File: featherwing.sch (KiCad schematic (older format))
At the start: 3 parts, among them J9 GROVE-SMD-90D, U1 ROF-78E

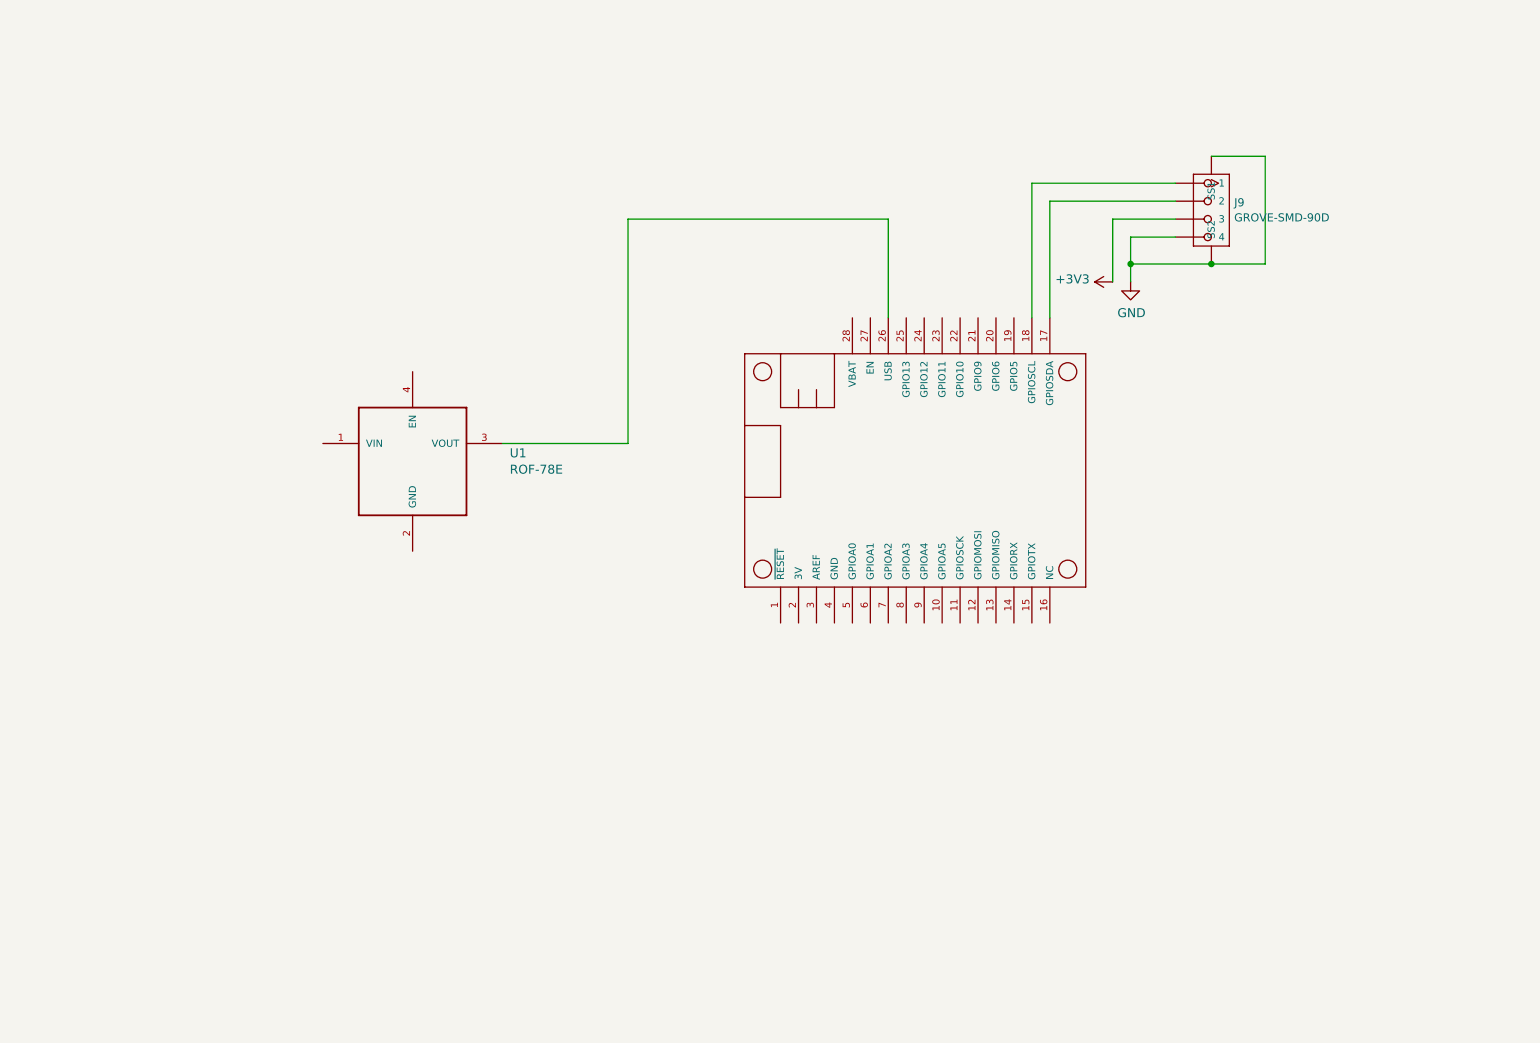
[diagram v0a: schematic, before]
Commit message: Updates from urbito, wired up featherwing
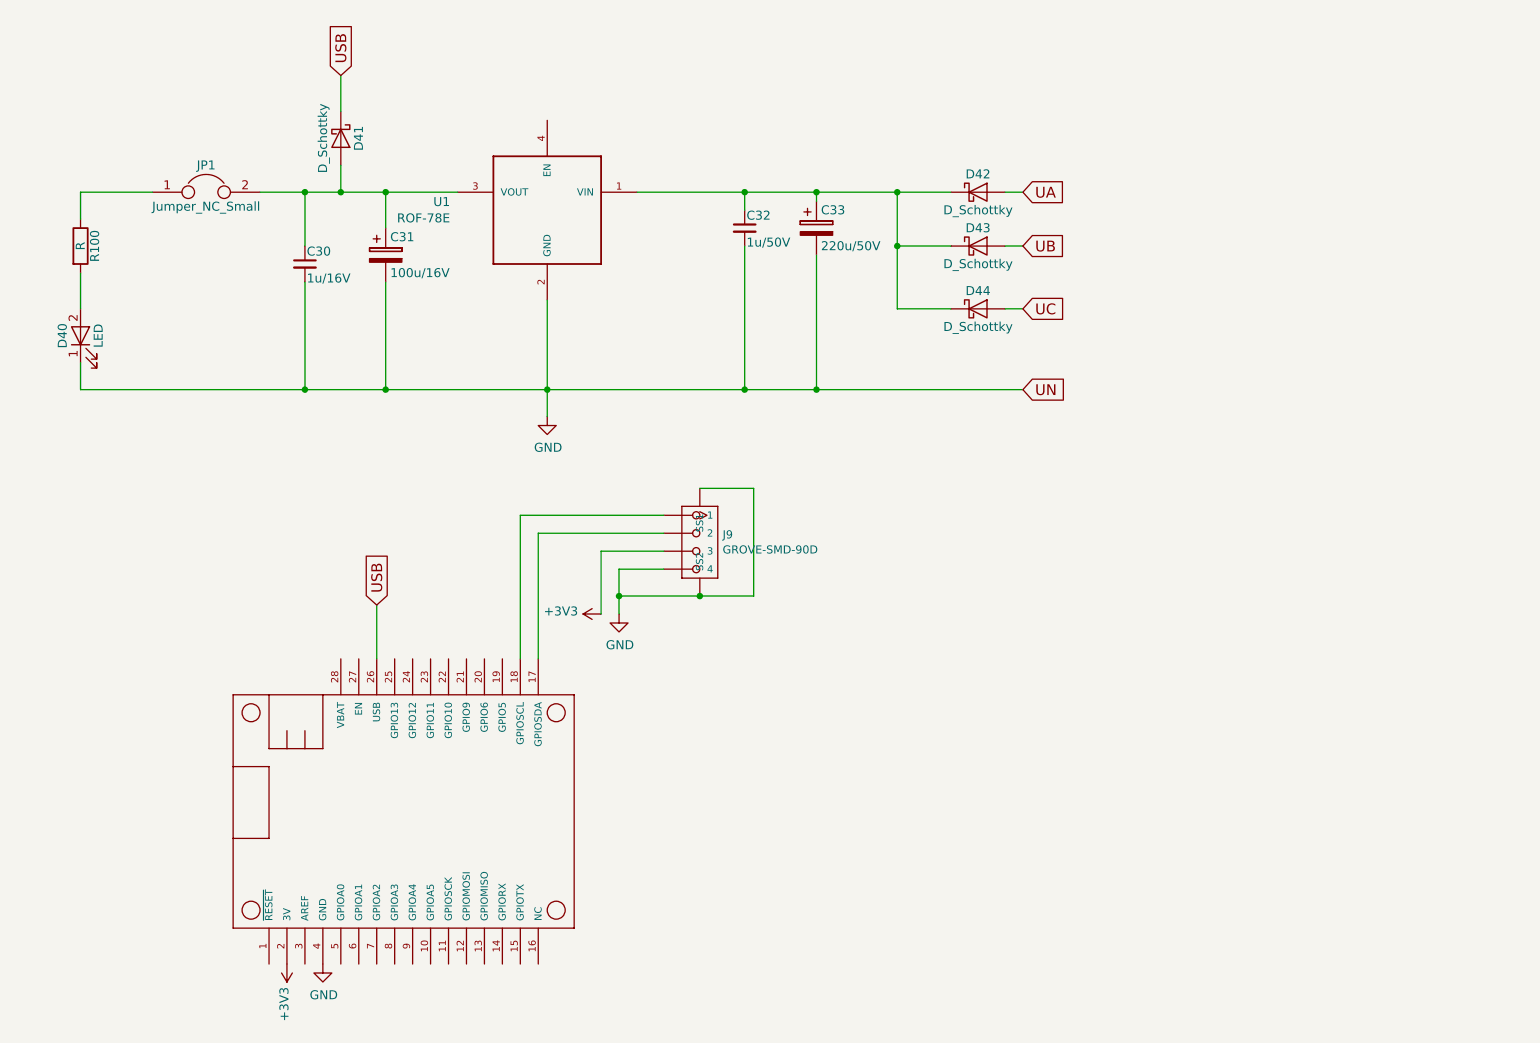
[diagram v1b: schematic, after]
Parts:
- added C30: 1u/16V, Capacitors_SMD:C_0603, symbol C_Small
- added C31: 100u/16V, Capacitors_SMD:CP_Elec_5x5.8, symbol CP
- added C32: 1u/50V, Capacitors_SMD:C_0603, symbol C_Small
- added C33: 220u/50V, Capacitors_SMD:CP_Elec_8x10, symbol CP
- added D40: LED, LEDs:LED_0603, symbol LED
- added D41, D42, D43, D44: D_Schottky, Diodes_SMD:D_SOD-123, symbol D_Schottky
- added JP1: Jumper_NC_Small, Connect:GS2, symbol Jumper
- added R100: R, Resistors_SMD:R_0603_HandSoldering, symbol R
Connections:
- net +3V3: now also MS1.2 (3V)
- net GND: now also MS1.4 (GND), U1.2 (GND), C30.2, C31.2, C32.2, C33.2, D40.1 (K)
- net at U1.1 (VIN): now also C32.1, C33.1, D42.1 (K), D43.1 (K), D44.1 (K)
- net at U1.3 (VOUT): now also C30.1, C31.1, D41.2 (A), JP1.2; no longer MS1.26 (USB)
- new net: D40.2 (A), R100.2
- new net: JP1.1, R100.1
- new net UA: D42.2 (A)
- new net UB: D43.2 (A)
- new net UC: D44.2 (A)
- new net USB: D41.1 (K), MS1.26 (USB)
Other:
- moved on the sheet: J9, U1

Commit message: Urbito delivery
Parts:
- added J10: CONN_01X06, Connectors_JST:JST_SH_SM06B-SRSS-TB_06x1.00mm_Angled, symbol CONN_01X06
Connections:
- net +3V3: now also J10.5 (P5); no longer MS1.2 (3V)
- net GND: now also J10.6 (P6); no longer MS1.4 (GND)
- new net CS: J10.1 (P1)
- new net MISO: J10.2 (P2)
- new net MOSI: J10.3 (P3)
- new net SCK: J10.4 (P4)
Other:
- moved on the sheet: J9
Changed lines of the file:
@@
 LIBS:ROF-78E
 LIBS:ATM90E26_Featherwing
+LIBS:logo
 LIBS:ATM90E3x_fw-cache
-EELAYER 26 0
+EELAYER 25 0
 EELAYER END
 $Descr A4 11693 8268
@@
 L ADAFRUIT_FEATHERWING MS1
 U 1 1 59441A98
-P 3600 5950
-F 0 "MS1" H 3600 5950 45  0001 C CNN
-F 1 "ADAFRUIT_FEATHERWING" H 3600 5950 45  0001 C CNN
-F 2 "ATM90E26_from_eagle:ADAFRUIT_FEATHERWING" H 3600 5950 60  0001 C CNN
-F 3 "" H 3600 5950 60  0001 C CNN
-	1    3600 5950
+P 7400 5900
+F 0 "MS1" H 7400 5900 45  0001 C CNN
+F 1 "ADAFRUIT_FEATHERWING" H 7400 5900 45  0001 C CNN
+F 2 "ATM90E26_from_eagle:ADAFRUIT_FEATHERWING" H 7400 5900 60  0001 C CNN
+F 3 "" H 7400 5900 60  0001 C CNN
+	1    7400 5900
 	1    0    0    -1
 $EndComp
@@
 L SEEED-CONNECTOR--2016_GROVE-CONNECTOR-SMD-90D_4+2P-2.0_ J9
 U 1 1 59469847
-P 6200 3800
-F 0 "J9" H 6327 3842 45  0000 L CNN
-F 1 "GROVE-SMD-90D" H 6327 3758 45  0000 L CNN
-F 2 "ATM90E26_from_eagle:SEEED-CONNECTOR--2016_HW4-SMD-2.0-90D" H 6200 3800 60  0001 C CNN
-F 3 "" H 6200 3800 60  0001 C CNN
-	1    6200 3800
+P 10000 3750
+F 0 "J9" H 10127 3792 45  0000 L CNN
+F 1 "GROVE-SMD-90D" H 10127 3708 45  0000 L CNN
+F 2 "ATM90E26_from_eagle:SEEED-CONNECTOR--2016_HW4-SMD-2.0-90D" H 10000 3750 60  0001 C CNN
+F 3 "" H 10000 3750 60  0001 C CNN
+	1    10000 3750
 	1    0    0    -1
 $EndComp
@@
 L +3V3 #PWR017
 U 1 1 5946B9F0
-P 5650 4200
-F 0 "#PWR017" H 5650 4050 50  0001 C CNN
-F 1 "+3V3" V 5665 4328 50  0000 L CNN
-F 2 "" H 5650 4200 50  0001 C CNN
-F 3 "" H 5650 4200 50  0001 C CNN
-	1    5650 4200
+P 9450 4150
+F 0 "#PWR017" H 9450 4000 50  0001 C CNN
+F 1 "+3V3" V 9465 4278 50  0000 L CNN
+F 2 "" H 9450 4150 50  0001 C CNN
+F 3 "" H 9450 4150 50  0001 C CNN
+	1    9450 4150
 	0    -1   -1   0
 $EndComp
@@
 L GND #PWR018
 U 1 1 5946BA31
-P 5750 4200
-F 0 "#PWR018" H 5750 3950 50  0001 C CNN
-F 1 "GND" H 5755 4027 50  0000 C CNN
-F 2 "" H 5750 4200 50  0001 C CNN
-F 3 "" H 5750 4200 50  0001 C CNN
-	1    5750 4200
-	1    0    0    -1
+P 9550 4150
+F 0 "#PWR018" H 9550 3900 50  0001 C CNN
+F 1 "GND" H 9555 3977 50  0000 C CNN
+F 2 "" H 9550 4150 50  0001 C CNN
+F 3 "" H 9550 4150 50  0001 C CNN
+	1    9550 4150
+	1    0    0    -1
+$EndComp
+$Comp
+L CONN_01X06 J10
+U 1 1 59558551
+P 3300 4100
+F 0 "J10" H 3300 4450 50  0000 C CNN
+F 1 "CONN_01X06" V 3400 4100 50  0000 C CNN
+F 2 "Connectors_JST:JST_SH_SM06B-SRSS-TB_06x1.00mm_Angled" H 3300 4100 50  0001 C CNN
+F 3 "" H 3300 4100 50  0001 C CNN
+	1    3300 4100
+	1    0    0    1
 $EndComp
 $Comp
@@
 Text GLabel 4200 1200 1    60   Input ~ 0
 USB
-Text GLabel 4400 4150 1    60   Input ~ 0
+Text GLabel 8200 4100 1    60   Input ~ 0
 USB
 Text GLabel 8000 2950 2    60   Input ~ 0
@@
 $EndComp
 Wire Wire Line
-	5200 3650 6000 3650
-Wire Wire Line
-	6000 3850 5650 3850
-Wire Wire Line
-	5650 3850 5650 4200
-Wire Wire Line
-	6000 3950 5750 3950
-Wire Wire Line
-	5750 3950 5750 4200
-Wire Wire Line
-	5750 4100 6500 4100
-Connection ~ 5750 4100
-Wire Wire Line
-	6200 3500 6500 3500
-Wire Wire Line
-	6500 3500 6500 4100
-Connection ~ 6200 4100
-Wire Wire Line
-	5200 3650 5200 4450
-Wire Wire Line
-	5300 4450 5300 3750
-Wire Wire Line
-	5300 3750 6000 3750
+	9000 3600 9800 3600
+Wire Wire Line
+	9800 3800 9450 3800
+Wire Wire Line
+	9450 3800 9450 4150
+Wire Wire Line
+	9800 3900 9550 3900
+Wire Wire Line
+	9550 3900 9550 4150
+Wire Wire Line
+	9550 4050 10300 4050
+Connection ~ 9550 4050
+Wire Wire Line
+	10000 3450 10300 3450
+Wire Wire Line
+	10300 3450 10300 4050
+Connection ~ 10000 4050
+Wire Wire Line
+	9000 3600 9000 4400
+Wire Wire Line
+	9100 4400 9100 3700
+Wire Wire Line
+	9100 3700 9800 3700
 Wire Wire Line
 	3750 1850 4850 1850
@@
 	4200 1400 4200 1200
 Wire Wire Line
-	4400 4450 4400 4150
+	8200 4400 8200 4100
 Connection ~ 6850 1850
 Wire Wire Line
@@
 Wire Wire Line
 	8000 2500 7900 2500
-$Comp
-L +3V3 #PWR?
-U 1 1 5964CF52
-P 3900 6150
-F 0 "#PWR?" H 3900 6000 50  0001 C CNN
-F 1 "+3V3" V 3915 6278 50  0000 L CNN
-F 2 "" H 3900 6150 50  0001 C CNN
-F 3 "" H 3900 6150 50  0001 C CNN
-	1    3900 6150
-	-1   0    0    1
-$EndComp
-$Comp
-L GND #PWR?
-U 1 1 5964CF9E
-P 4100 6150
-F 0 "#PWR?" H 4100 5900 50  0001 C CNN
-F 1 "GND" H 4105 5977 50  0000 C CNN
-F 2 "" H 4100 6150 50  0001 C CNN
-F 3 "" H 4100 6150 50  0001 C CNN
-	1    4100 6150
-	1    0    0    -1
-$EndComp
+Text GLabel 2800 3850 0    60   Input ~ 0
+GND
+Text GLabel 2800 3950 0    60   Input ~ 0
++3V3
+Text GLabel 2800 4050 0    60   Input ~ 0
+SCK
+Text GLabel 2800 4150 0    60   Input ~ 0
+MOSI
+Text GLabel 2800 4250 0    60   Input ~ 0
+MISO
+Text GLabel 2800 4350 0    60   Input ~ 0
+CS
+Wire Wire Line
+	3100 3850 2800 3850
+Wire Wire Line
+	3100 3950 2800 3950
+Wire Wire Line
+	3100 4050 2800 4050
+Wire Wire Line
+	3100 4150 2800 4150
+Wire Wire Line
+	3100 4250 2800 4250
+Wire Wire Line
+	3100 4350 2800 4350
 $EndSCHEMATC
